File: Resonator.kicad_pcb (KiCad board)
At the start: 2 copper layers, 45 parts, among them U1 TL074, U2 PCM3060

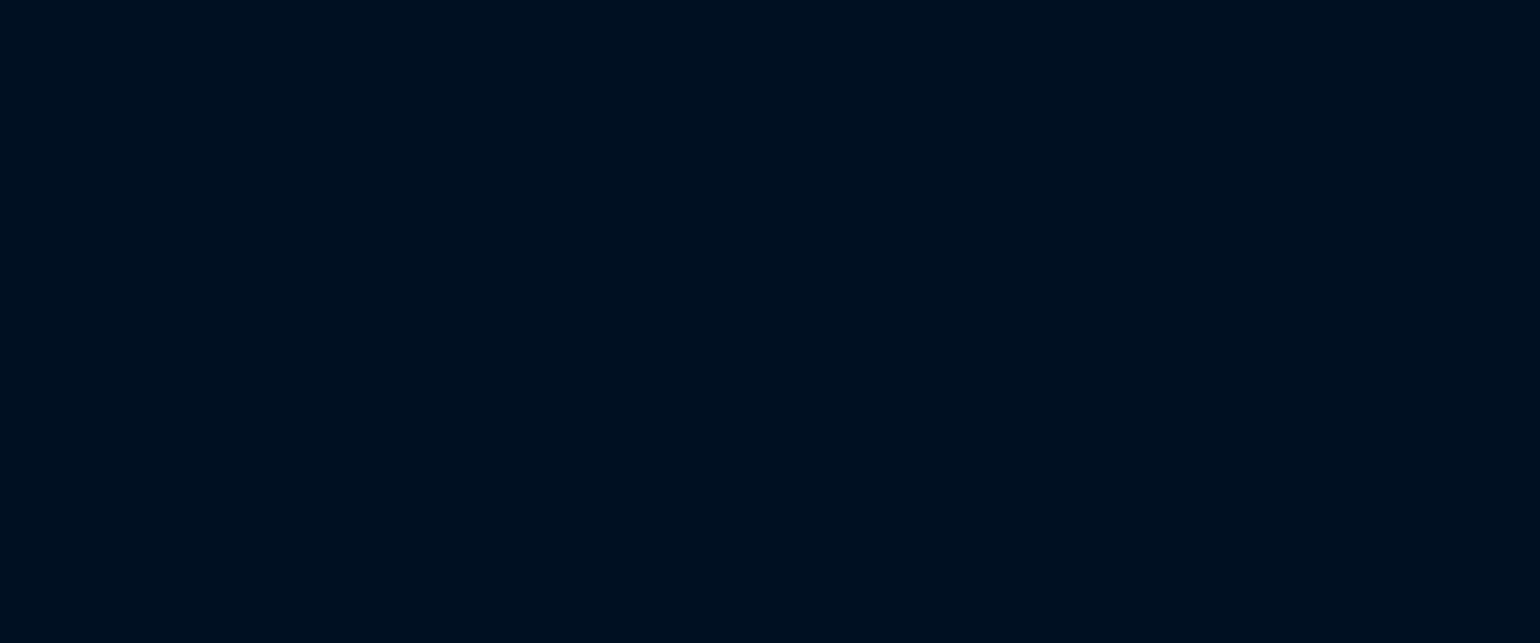
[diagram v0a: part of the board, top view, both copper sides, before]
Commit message: Added power supply and adjusted gains for 12Vpp I/O.
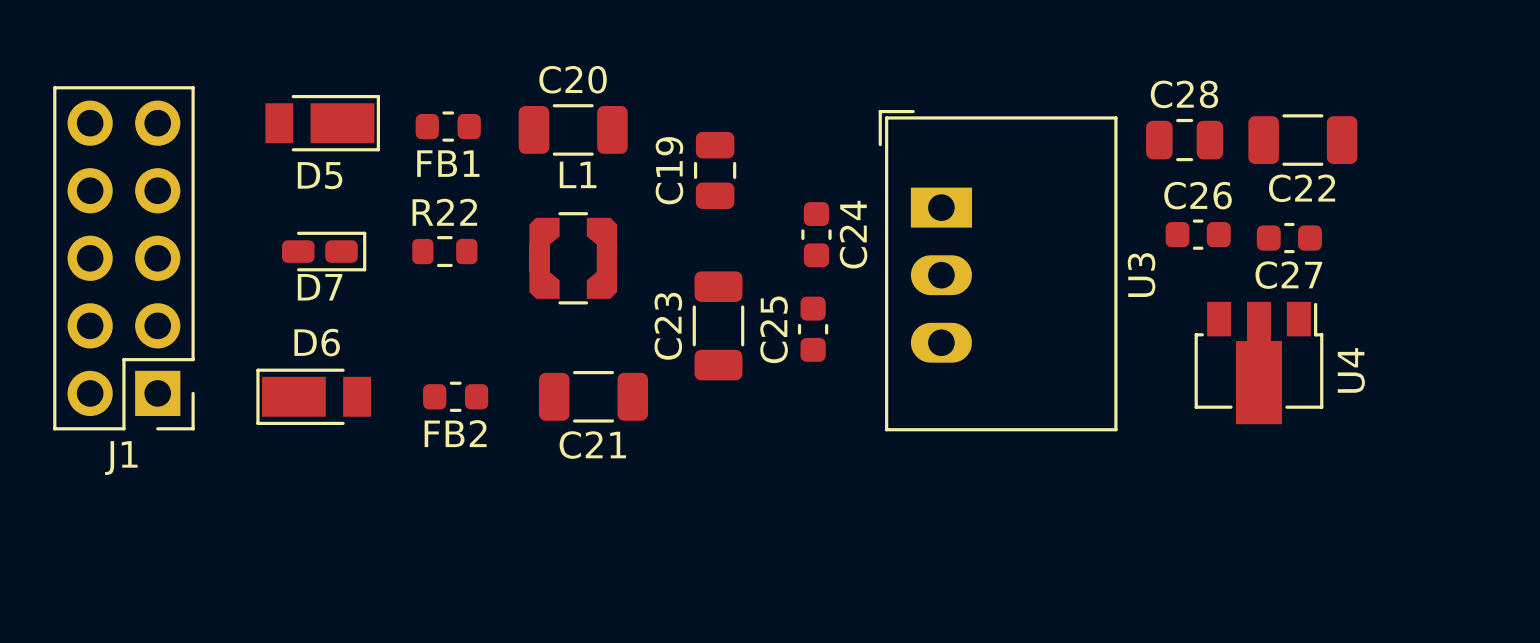
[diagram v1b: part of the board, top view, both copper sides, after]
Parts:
- added C19: 4u7, Capacitor_SMD:C_0805_2012Metric, F.Cu at (44.6, 27.6)
- added C20: 22u, Capacitor_SMD:C_1206_3216Metric, F.Cu at (39.2, 26.0)
- added C21: 22u, Capacitor_SMD:C_1206_3216Metric, F.Cu at (40.0, 36.1)
- added C22: 22u, Capacitor_SMD:C_1206_3216Metric, F.Cu at (66.7, 26.4)
- added C23: 22u, Capacitor_SMD:C_1206_3216Metric, F.Cu at (44.7, 33.4)
- added C24: 100n, Capacitor_SMD:C_0603_1608Metric, F.Cu at (48.4, 30.0)
- added C25: 100n, Capacitor_SMD:C_0603_1608Metric, F.Cu at (48.3, 33.5)
- added C26: 100n, Capacitor_SMD:C_0603_1608Metric, F.Cu at (62.7, 30.0)
- added C27: 100n, Capacitor_SMD:C_0603_1608Metric, F.Cu at (66.2, 30.1)
- added C28: 4u7, Capacitor_SMD:C_0805_2012Metric, F.Cu at (62.2, 26.4)
- added D5: DFLR1400-7, Diode_SMD:D_PowerDI-123, F.Cu at (29.7, 25.8)
- added D6: DFLR1400-7, Diode_SMD:D_PowerDI-123, F.Cu at (29.6, 36.1)
- added D7: LED, LED_SMD:LED_0603_1608Metric_Castellated, F.Cu at (29.7, 30.6)
- added FB1: Ferrite_Bead, Inductor_SMD:L_0603_1608Metric, F.Cu at (34.5, 25.9)
- added FB2: Ferrite_Bead, Inductor_SMD:L_0603_1608Metric, F.Cu at (34.8, 36.1)
- added J1: Conn_02x05_Odd_Even, Connector_PinHeader_2.54mm:PinHeader_2x05_P2.54mm_Vertical, F.Cu at (23.6, 35.9)
- added L1: 12u, Local:L_Coilcraft_LPS3010, F.Cu at (39.2, 30.9)
- added R22: 1k, Resistor_SMD:R_0603_1608Metric, F.Cu at (34.4, 30.6)
- added U3: R-78E5.0-0.5, Converter_DCDC:Converter_DCDC_RECOM_R-78E-0.5_THT, F.Cu at (53.1, 29.0)
- added U4: LD2981ABU33TR, Package_TO_SOT_SMD:SOT-89-3, F.Cu at (65.0, 34.8)
- C8, C9: value 120p -> 150p
- R12, R5, R8, R9: value 25k -> 15k
- R15, R16: value 30k -> 25k

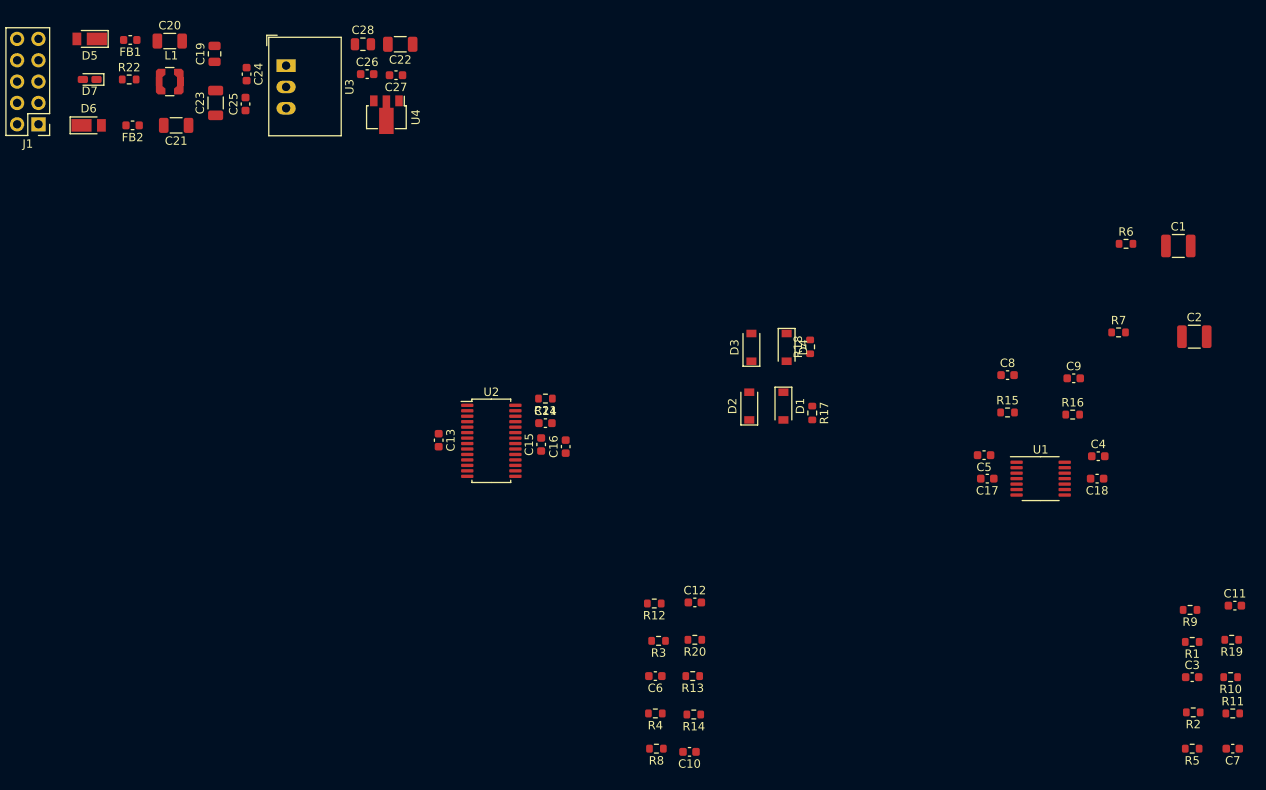
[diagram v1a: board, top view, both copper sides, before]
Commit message: Moved audio-io to separate sheet.
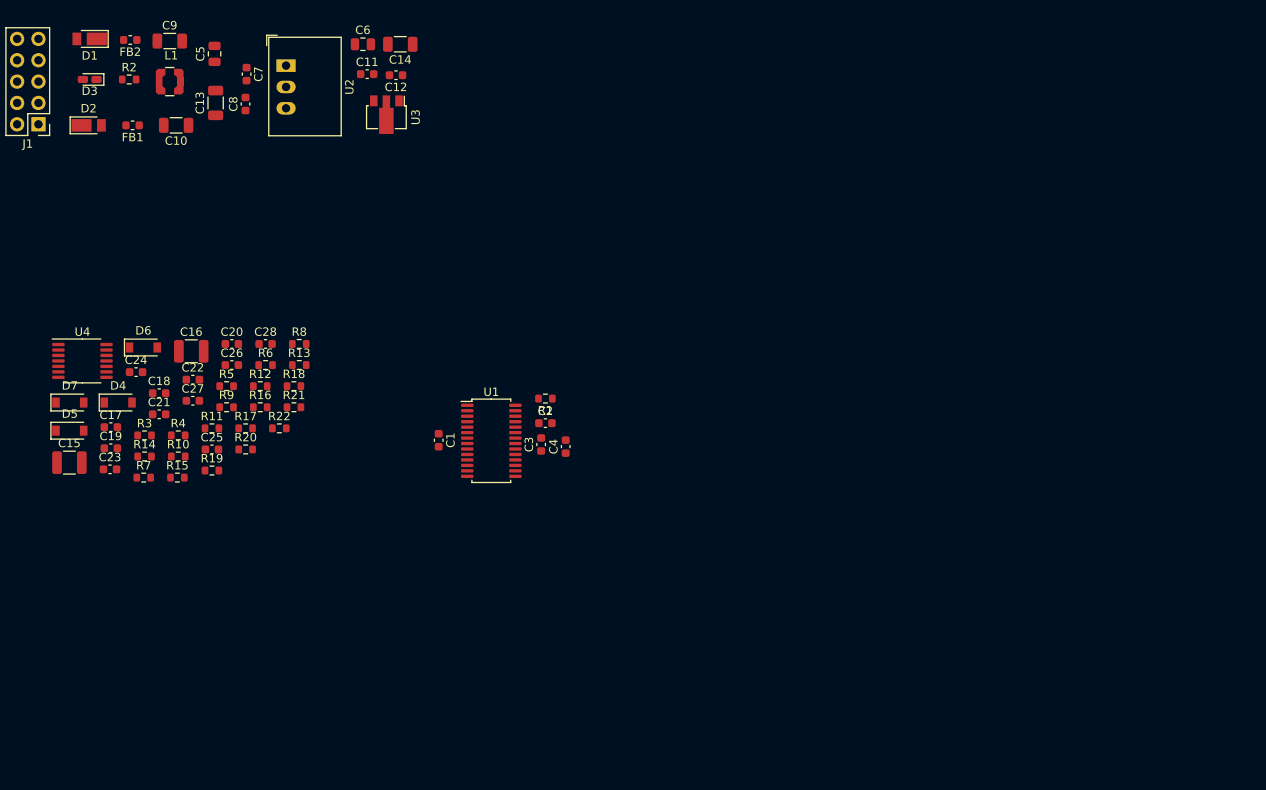
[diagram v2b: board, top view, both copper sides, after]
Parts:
- removed the C1 at (159.3, 50.4)
- removed the C10 at (101.1, 110.6)
- removed the C11 at (166.0, 93.2)
- removed the C12 at (101.7, 92.8)
- removed the C2 at (161.2, 61.2)
- removed the C3 at (160.9, 101.7)
- removed the C4 at (149.7, 75.4)
- removed the C5 at (136.1, 75.3)
- removed the C6 at (97.0, 101.6)
- removed the C7 at (165.7, 110.2)
- removed the C8 at (138.9, 65.8)
- removed the C9 at (146.8, 66.2)
- removed the D1 at (112.3, 69.5)
- removed the D2 at (108.2, 69.5)
- removed the D3 at (108.5, 62.5)
- removed the R1 at (160.9, 97.5)
- removed the R2 at (161.0, 105.9)
- removed the U1 at (142.9, 78.1)
- added C15: 1u, Capacitor_SMD:C_1210_3225Metric, F.Cu at (27.3, 76.2)
- added C16: 1u, Capacitor_SMD:C_1210_3225Metric, F.Cu at (41.8, 63.0)
- added C19: 100n, Capacitor_SMD:C_0603_1608Metric, F.Cu at (32.2, 74.5)
- added C20: 100n, Capacitor_SMD:C_0603_1608Metric, F.Cu at (46.6, 62.1)
- added C21: 150p, Capacitor_SMD:C_0603_1608Metric, F.Cu at (38.0, 70.5)
- added C22: 150p, Capacitor_SMD:C_0603_1608Metric, F.Cu at (42.0, 66.3)
- added C23: 1n5, Capacitor_SMD:C_0603_1608Metric, F.Cu at (32.1, 77.0)
- added C24: 1n5, Capacitor_SMD:C_0603_1608Metric, F.Cu at (35.2, 65.4)
- added C25: 470p, Capacitor_SMD:C_0603_1608Metric, F.Cu at (44.3, 74.6)
- added C26: 470p, Capacitor_SMD:C_0603_1608Metric, F.Cu at (46.6, 64.6)
- added C27: 470p, Capacitor_SMD:C_0603_1608Metric, F.Cu at (42.0, 68.8)
- added C28: 470p, Capacitor_SMD:C_0603_1608Metric, F.Cu at (50.6, 62.1)
- added D5: 1N5819, Diode_SMD:D_SOD-123, F.Cu at (27.4, 72.4)
- added D6: 1N5819, Diode_SMD:D_SOD-123, F.Cu at (36.1, 62.5)
- added D7: 1N5819, Diode_SMD:D_SOD-123, F.Cu at (27.4, 69.0)
- added R21: 1k, Resistor_SMD:R_0603_1608Metric, F.Cu at (54.0, 69.6)
- added R22: 1k, Resistor_SMD:R_0603_1608Metric, F.Cu at (52.3, 72.1)
- added U4: TL074, Package_SO:TSSOP-14_4.4x5mm_P0.65mm, F.Cu at (28.9, 64.1)
- R10, R11: value 820 -> 10k
- R12, R9: value 15k -> 10k
- R13, R14: value 820 -> 15k
- R15: value 25k -> 15k
- R16: value 25k -> 820
- R17, R19, R20: value 1k -> 820
- R18: value 1k -> 15k
- R3, R4: value 10k -> 100k
- R5: value 15k -> 25k
- R6: value 100k -> 25k
- R7: value 100k -> 1k
- R8: value 15k -> 1k
- moved R10 127.9 mm to (40.3, 75.5), turned to 0 degrees
- moved R11 126.1 mm to (44.3, 72.1)
- moved R19 123.0 mm to (44.3, 77.1), turned to 0 degrees
- moved R5 122.7 mm to (46.0, 67.1), turned to 0 degrees
- moved R7 117.3 mm to (36.1, 78.0)
- moved R9 117.2 mm to (46.0, 69.6), turned to 0 degrees
- moved C18 112.1 mm to (38.0, 67.9), turned to 0 degrees
- moved C17 104.5 mm to (32.2, 72.0), turned to 0 degrees
- moved R6 103.4 mm to (50.6, 64.6)
- moved R15 99.1 mm to (40.2, 78.0)
- moved R16 96.7 mm to (50.0, 69.6)
- moved D4 79.8 mm to (33.1, 69.0), turned to 0 degrees
- moved R14 72.2 mm to (36.2, 75.5), turned to 0 degrees
- moved R17 67.4 mm to (48.3, 72.1), turned to 0 degrees
- moved R3 65.9 mm to (36.2, 73.0), turned to 0 degrees
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- renumbered C13 to C1, C21 to C10, C26 to C11, C27 to C12, C23 to C13, C22 to C14, C14 to C2, C15 to C3, C16 to C4, C19 to C5, C28 to C6, C24 to C7, C25 to C8, C20 to C9, D5 to D1, D6 to D2, D7 to D3, FB2 to FB1, FB1 to FB2, R21 to R1, R22 to R2, U2 to U1, U3 to U2, U4 to U3
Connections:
- C17 pad 1: +12V -> VCom
- C18 pad 1: GND -> VCom
- C18 pad 2: -12V -> GND
- D4 pad 1: VinR -> +5V
- D4 pad 2: GND -> VinL
- R10 pad 1: Net-(C11-Pad2) -> Net-(C23-Pad2)
- R10 pad 2: Net-(C3-Pad1) -> VOutR-
- R11 pad 1: Net-(C7-Pad1) -> Net-(C24-Pad1)
- R11 pad 2: Net-(C3-Pad2) -> VOutL+
- R12 pad 1: Net-(C12-Pad1) -> Net-(C24-Pad2)
- R12 pad 2: Net-(C6-Pad1) -> VOutL-
- R13 pad 1: Net-(C12-Pad2) -> GND
- R13 pad 2: Net-(C6-Pad1) -> Net-(C23-Pad2)
- R14 pad 1: Net-(C10-Pad1) -> GND
- R14 pad 2: Net-(C6-Pad2) -> Net-(C24-Pad2)
- R15 pad 1: Net-(C8-Pad1) -> Net-(C27-Pad1)
- R15 pad 2: Net-(C8-Pad2) -> Net-(C23-Pad1)
- R16 pad 1: Net-(C9-Pad1) -> Net-(C27-Pad2)
- R16 pad 2: Net-(C9-Pad2) -> Net-(C23-Pad1)
- R17 pad 1: Net-(C8-Pad1) -> Net-(C25-Pad1)
- R17 pad 2: VinL -> Net-(C23-Pad2)
- R18 pad 1: Net-(C9-Pad1) -> Net-(C28-Pad1)
- R18 pad 2: VinR -> Net-(C24-Pad1)
- R19 pad 1: OutR -> Net-(C28-Pad2)
- R19 pad 2: Net-(C11-Pad1) -> Net-(C24-Pad1)
- R20 pad 1: OutL -> Net-(C26-Pad1)
- R20 pad 2: Net-(C12-Pad1) -> Net-(C24-Pad2)
- R3 pad 1: Net-(C6-Pad1) -> Net-(C21-Pad2)
- R3 pad 2: VOutL+ -> Net-(C15-Pad1)
- R4 pad 1: Net-(C6-Pad2) -> Net-(C22-Pad2)
- R4 pad 2: VOutL- -> Net-(C16-Pad1)
- R5 pad 1: GND -> Net-(C21-Pad1)
- R5 pad 2: Net-(C3-Pad2) -> Net-(C21-Pad2)
- R6 pad 1: Net-(C8-Pad2) -> Net-(C22-Pad1)
- R6 pad 2: Net-(C1-Pad1) -> Net-(C22-Pad2)
- R7 pad 1: Net-(C9-Pad2) -> Net-(C21-Pad1)
- R7 pad 2: Net-(C2-Pad1) -> VinL
- R8 pad 1: GND -> Net-(C22-Pad1)
- R8 pad 2: Net-(C6-Pad2) -> VinR
- R9 pad 1: Net-(C11-Pad1) -> Net-(C23-Pad1)
- R9 pad 2: Net-(C3-Pad1) -> VOutR+

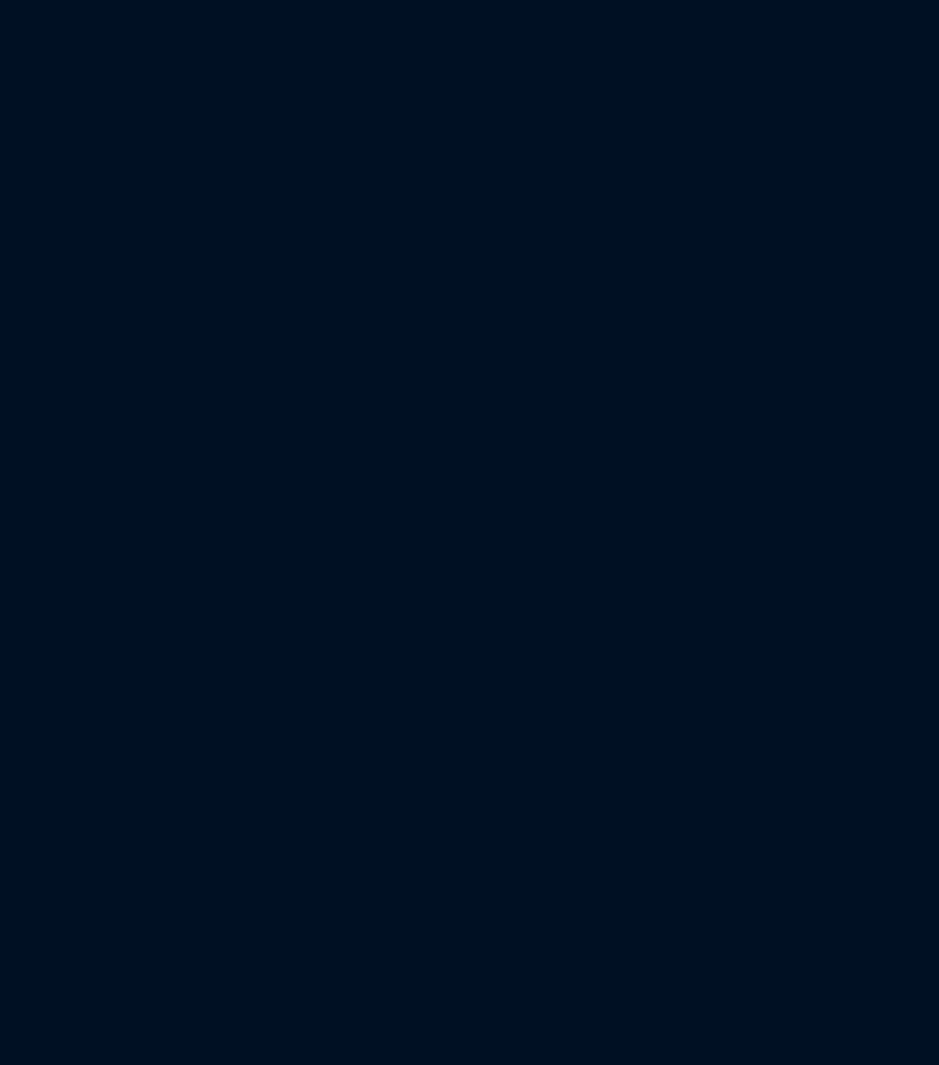
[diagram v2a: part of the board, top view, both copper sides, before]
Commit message: Added STM32750 mcu.
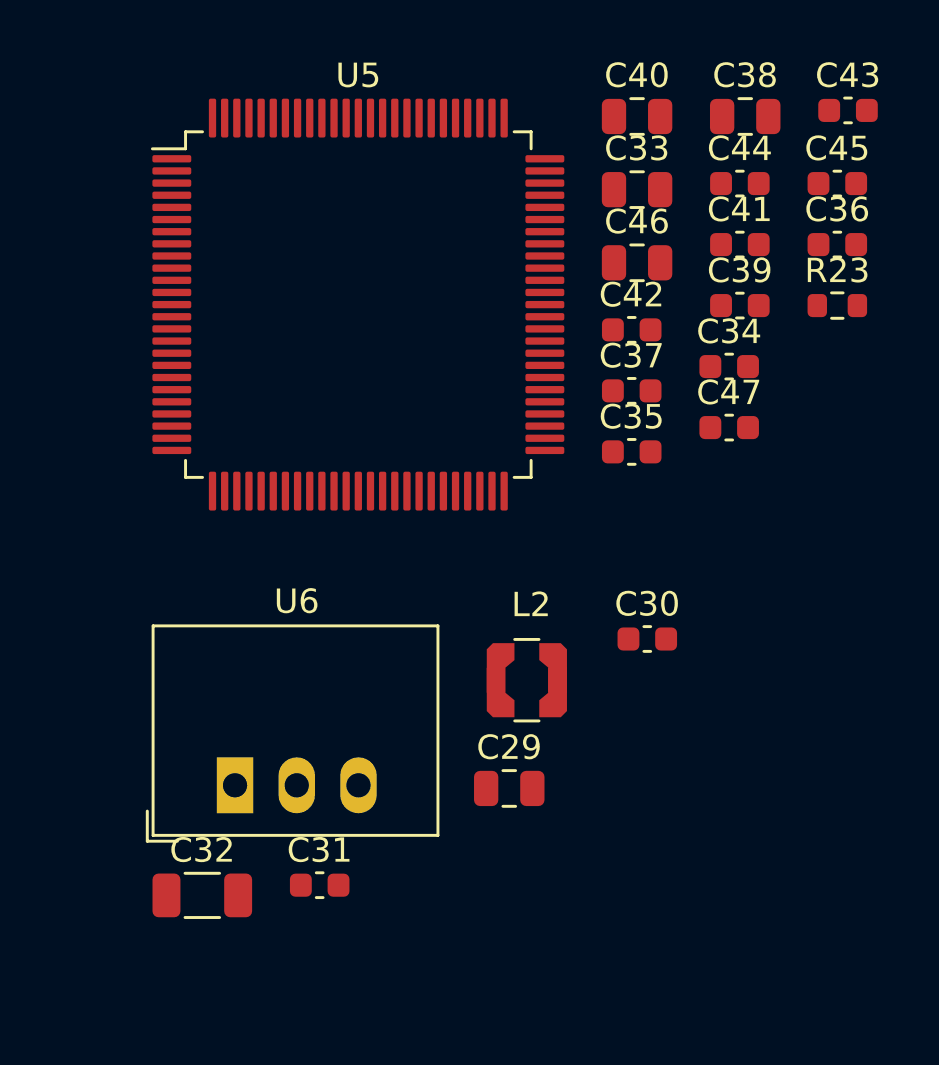
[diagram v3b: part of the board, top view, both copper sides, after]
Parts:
- added C29: 4u7, Capacitor_SMD:C_0805_2012Metric, F.Cu at (100.7, 53.6)
- added C30: 100n, Capacitor_SMD:C_0603_1608Metric, F.Cu at (106.4, 47.4)
- added C31: 100n, Capacitor_SMD:C_0603_1608Metric, F.Cu at (92.9, 57.6)
- added C32: 22u, Capacitor_SMD:C_1206_3216Metric, F.Cu at (88.1, 58.0)
- added C33: 4u7, Capacitor_SMD:C_0805_2012Metric, F.Cu at (106.0, 29.0)
- added C34: 100n, Capacitor_SMD:C_0603_1608Metric, F.Cu at (109.8, 36.2)
- added C35: 100n, Capacitor_SMD:C_0603_1608Metric, F.Cu at (105.8, 39.7)
- added C36: 100n, Capacitor_SMD:C_0603_1608Metric, F.Cu at (114.2, 31.2)
- added C37: 100n, Capacitor_SMD:C_0603_1608Metric, F.Cu at (105.8, 37.2)
- added C38: 2u2, Capacitor_SMD:C_0805_2012Metric, F.Cu at (110.4, 25.9)
- added C39: 100n, Capacitor_SMD:C_0603_1608Metric, F.Cu at (110.2, 33.7)
- added C40: 2u2, Capacitor_SMD:C_0805_2012Metric, F.Cu at (106.0, 25.9)
- added C41: 3p9, Capacitor_SMD:C_0603_1608Metric, F.Cu at (110.2, 31.2)
- added C42: 3p9, Capacitor_SMD:C_0603_1608Metric, F.Cu at (105.8, 34.7)
- added C43: 100n, Capacitor_SMD:C_0603_1608Metric, F.Cu at (114.7, 25.7)
- added C44: 100n, Capacitor_SMD:C_0603_1608Metric, F.Cu at (110.2, 28.7)
- added C45: 100n, Capacitor_SMD:C_0603_1608Metric, F.Cu at (114.2, 28.7)
- added C46: 1u, Capacitor_SMD:C_0805_2012Metric, F.Cu at (106.0, 32.0)
- added C47: 100n, Capacitor_SMD:C_0603_1608Metric, F.Cu at (109.8, 38.7)
- added L2: 12u, Local:L_Coilcraft_LPS3010, F.Cu at (101.4, 49.1)
- added R23: 10k, Resistor_SMD:R_0603_1608Metric, F.Cu at (114.2, 33.7)
- added U5: STM32H750VBTx, Package_QFP:LQFP-100_14x14mm_P0.5mm, F.Cu at (94.5, 33.7)
- added U6: R-78E3.3-0.5, Converter_DCDC:Converter_DCDC_RECOM_R-78E-0.5_THT, F.Cu at (89.4, 53.5)
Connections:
- C12 pad 1: +3V3 -> +3.3VA
- C14 pad 1: +3V3 -> +3.3VA
- U3 pad 1: +3V3 -> +3.3VA
